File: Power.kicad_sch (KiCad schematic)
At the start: 12 parts

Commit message: finished power schematic
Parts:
- added C10, C11, C12, C9: 220pF, Capacitor_SMD:C_1210_3225Metric, symbol Device:C
- added Q1, Q2: IMZA65R050M2H, mosfets:TO247-4-Horizontal, symbol Library-N2-MOSFETs:IMZA65R050M2H
- added R1, R2: 50, Resistor_SMD:R_0805_2012Metric, symbol Device:R
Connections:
- net +15V_Top: no longer C8.1, PS2.6 (+Vo)
- net SW: now also Q1.2 (SOURCE1), Q2.1 (DRAIN); no longer C7.2, C8.2, PS2.4 (0V)
- new net: Q2.4 (GATE), R2.2
- new net: Q1.4 (GATE), R1.2
- new net +15V_Bot: C8.1, PS2.6 (+Vo)
- new net Bot_MOS_G: Q2.3 (SOURCE2), R2.1
- new net GNDPWR: C10.1, C11.1, C12.1, C7.2, C8.2, C9.1, PS2.4 (0V), Q2.2 (SOURCE1)
- new net HVBUS: C10.2, C11.2, C12.2, C9.2, Q1.1 (DRAIN)
- new net Top_MOS_G: Q1.3 (SOURCE2), R1.1
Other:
- moved on the sheet: C1, C2, C3, C4, C5, C6, C7, C8, L1, L2, PS1, PS2

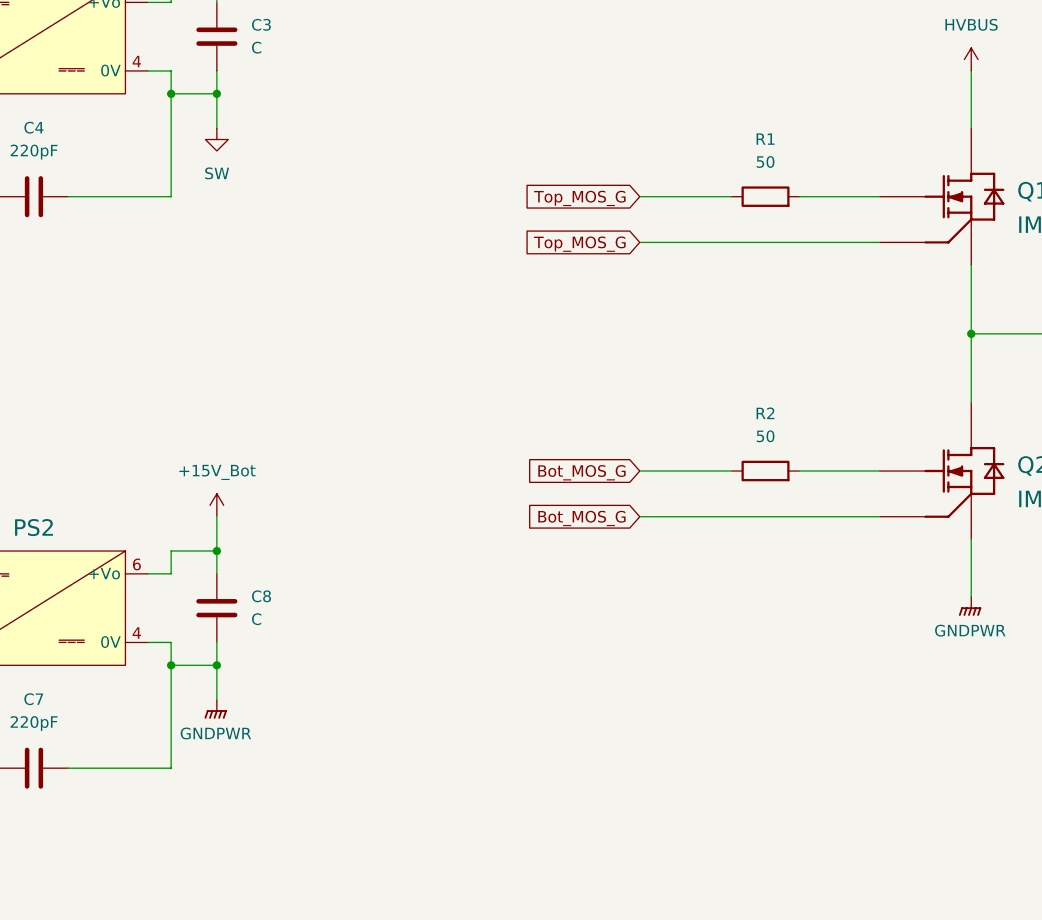
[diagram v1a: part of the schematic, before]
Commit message: gate driver added
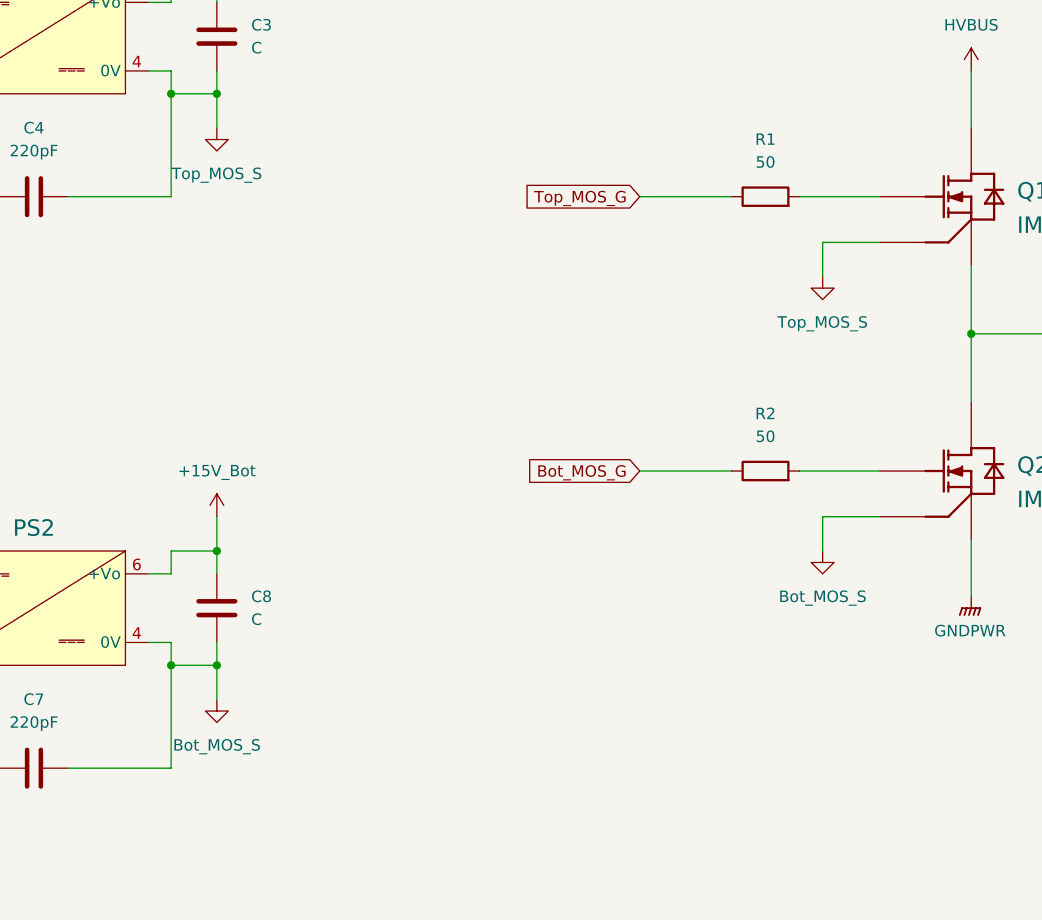
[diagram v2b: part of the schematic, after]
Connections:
- net Bot_MOS_G: no longer Q2.3 (SOURCE2)
- net GNDPWR: no longer C7.2, C8.2, PS2.4 (0V)
- net SW: no longer C3.2, C4.2, PS1.4 (0V)
- net Top_MOS_G: no longer Q1.3 (SOURCE2)
- new net Bot_MOS_S: C7.2, C8.2, PS2.4 (0V), Q2.3 (SOURCE2)
- new net Top_MOS_S: C3.2, C4.2, PS1.4 (0V), Q1.3 (SOURCE2)
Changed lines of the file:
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@@
+	(wire
+		(pts
+			(xy 198.12 107.95) (xy 204.47 107.95)
+		)
+		(stroke
+			(width 0)
+			(type default)
+		)
+	)
 	(wire
 		(pts
@@
 	(wire
 		(pts
+			(xy 198.12 77.47) (xy 204.47 77.47)
+		)
+		(stroke
+			(width 0)
+			(type default)
+		)
+	)
+	(wire
+		(pts
 			(xy 95.25 50.8) (xy 95.25 48.26)
 		)
@@
 	(wire
 		(pts
+			(xy 198.12 111.76) (xy 198.12 107.95)
+		)
+		(stroke
+			(width 0)
+			(type default)
+		)
+	)
+	(wire
+		(pts
 			(xy 123.19 114.3) (xy 125.73 114.3)
 		)
@@
 	(wire
 		(pts
+			(xy 198.12 81.28) (xy 198.12 77.47)
+		)
+		(stroke
+			(width 0)
+			(type default)
+		)
+	)
+	(wire
+		(pts
 			(xy 101.6 165.1) (xy 114.3 165.1)
 		)
@@
 	(wire
 		(pts
-			(xy 177.8 77.47) (xy 204.47 77.47)
-		)
-		(stroke
-			(width 0)
-			(type default)
-		)
-	)
-	(wire
-		(pts
 			(xy 130.81 111.76) (xy 130.81 107.95)
 		)
@@
 		(pts
 			(xy 101.6 175.26) (xy 101.6 177.8)
-		)
-		(stroke
-			(width 0)
-			(type default)
-		)
-	)
-	(wire
-		(pts
-			(xy 177.8 107.95) (xy 204.47 107.95)
 		)
 		(stroke
@@
 	(global_label "Bot_MOS_G"
 		(shape input)
-		(at 177.8 107.95 180)
+		(at 177.8 102.87 180)
 		(fields_autoplaced yes)
 		(effects
@@
 		)
 		(property "Intersheetrefs" "${INTERSHEET_REFS}"
-			(at 164.4735 107.95 0)
+			(at 164.4735 102.87 0)
 			(effects
 				(font
@@
 		)
 	)
-	(global_label "Bot_MOS_G"
+	(global_label "Top_MOS_G"
 		(shape input)
-		(at 177.8 102.87 180)
+		(at 177.8 72.39 180)
 		(fields_autoplaced yes)
 		(effects
@@
 		)
 		(property "Intersheetrefs" "${INTERSHEET_REFS}"
-			(at 164.4735 102.87 0)
+			(at 164.3526 72.39 0)
 			(effects
 				(font
@@
 		)
 	)
-	(global_label "Top_MOS_G"
+	(global_label "SW"
 		(shape input)
-		(at 177.8 72.39 180)
+		(at 229.87 87.63 0)
 		(fields_autoplaced yes)
 		(effects
@@
 				(size 1.27 1.27)
 			)
-			(justify right)
-		)
-		(property "Intersheetrefs" "${INTERSHEET_REFS}"
-			(at 164.3526 72.39 0)
-			(effects
-				(font
-					(size 1.27 1.27)
-				)
-				(justify right)
-				(hide yes)
-			)
-		)
-	)
-	(global_label "SW"
-		(shape input)
-		(at 229.87 87.63 0)
-		(fields_autoplaced yes)
-		(effects
-			(font
-				(size 1.27 1.27)
-			)
 			(justify left)
 		)
@@
 				)
 				(justify left)
-				(hide yes)
-			)
-		)
-	)
-	(global_label "Top_MOS_G"
-		(shape input)
-		(at 177.8 77.47 180)
-		(fields_autoplaced yes)
-		(effects
-			(font
-				(size 1.27 1.27)
-			)
-			(justify right)
-		)
-		(property "Intersheetrefs" "${INTERSHEET_REFS}"
-			(at 164.3526 77.47 0)
-			(effects
-				(font
-					(size 1.27 1.27)
-				)
-				(justify right)
 				(hide yes)
 			)
@@
 	)
 	(symbol
+		(lib_id "power:GND")
+		(at 198.12 81.28 0)
+		(unit 1)
+		(exclude_from_sim no)
+		(in_bom yes)
+		(on_board yes)
+		(dnp no)
+		(fields_autoplaced yes)
+		(property "Reference" "#PWR013"
+			(at 198.12 87.63 0)
+			(effects
+				(font
+					(size 1.27 1.27)
+				)
+				(hide yes)
+			)
+		)
+		(property "Value" "Top_MOS_S"
+			(at 198.12 86.36 0)
+			(effects
+				(font
+					(size 1.27 1.27)
+				)
+			)
+		)
+		(property "Footprint" ""
+			(at 198.12 81.28 0)
+			(effects
+				(font
+					(size 1.27 1.27)
+				)
+				(hide yes)
+			)
+		)
+		(property "Datasheet" ""
+			(at 198.12 81.28 0)
+			(effects
+				(font
+					(size 1.27 1.27)
+				)
+				(hide yes)
+			)
+		)
+		(property "Description" "Power symbol creates a global label with name \"GND\" , ground"
+			(at 198.12 81.28 0)
+			(effects
+				(font
+					(size 1.27 1.27)
+				)
+				(hide yes)
+			)
+		)
+		(pin "1"
+		)
+		(instances
+			(project "to247-4_card"
+				(path "/b6582af5-6107-4ea5-94ab-56651da9db37/c6f9b239-fb2c-4550-a056-6f105d804563"
+					(reference "#PWR013")
+					(unit 1)
+				)
+			)
+		)
+	)
+	(symbol
 		(lib_id "power:GNDPWR")
 		(at 214.63 116.84 0)
@@
 			)
 		)
-		(property "Value" "SW"
+		(property "Value" "Top_MOS_S"
 			(at 130.81 69.85 0)
 			(effects
@@
 				(path "/b6582af5-6107-4ea5-94ab-56651da9db37/c6f9b239-fb2c-4550-a056-6f105d804563"
 					(reference "#PWR04")
-					(unit 1)
-				)
-			)
-		)
-	)
-	(symbol
-		(lib_id "power:GNDPWR")
-		(at 130.81 128.27 0)
-		(unit 1)
-		(exclude_from_sim no)
-		(in_bom yes)
-		(on_board yes)
-		(dnp no)
-		(fields_autoplaced yes)
-		(property "Reference" "#PWR08"
-			(at 130.81 133.35 0)
-			(effects
-				(font
-					(size 1.27 1.27)
-				)
-				(hide yes)
-			)
-		)
-		(property "Value" "GNDPWR"
-			(at 130.683 132.08 0)
-			(effects
-				(font
-					(size 1.27 1.27)
-				)
-			)
-		)
-		(property "Footprint" ""
-			(at 130.81 129.54 0)
-			(effects
-				(font
-					(size 1.27 1.27)
-				)
-				(hide yes)
-			)
-		)
-		(property "Datasheet" ""
-			(at 130.81 129.54 0)
-			(effects
-				(font
-					(size 1.27 1.27)
-				)
-				(hide yes)
-			)
-		)
-		(property "Description" "Power symbol creates a global label with name \"GNDPWR\" , global ground"
-			(at 130.81 128.27 0)
-			(effects
-				(font
-					(size 1.27 1.27)
-				)
-				(hide yes)
-			)
-		)
-		(pin "1"
-		)
-		(instances
-			(project ""
-				(path "/b6582af5-6107-4ea5-94ab-56651da9db37/c6f9b239-fb2c-4550-a056-6f105d804563"
-					(reference "#PWR08")
 					(unit 1)
 				)
@@
 	)
 	(symbol
+		(lib_id "power:GND")
+		(at 130.81 128.27 0)
+		(unit 1)
+		(exclude_from_sim no)
+		(in_bom yes)
+		(on_board yes)
+		(dnp no)
+		(fields_autoplaced yes)
+		(property "Reference" "#PWR08"
+			(at 130.81 134.62 0)
+			(effects
+				(font
+					(size 1.27 1.27)
+				)
+				(hide yes)
+			)
+		)
+		(property "Value" "Bot_MOS_S"
+			(at 130.81 133.35 0)
+			(effects
+				(font
+					(size 1.27 1.27)
+				)
+			)
+		)
+		(property "Footprint" ""
+			(at 130.81 128.27 0)
+			(effects
+				(font
+					(size 1.27 1.27)
+				)
+				(hide yes)
+			)
+		)
+		(property "Datasheet" ""
+			(at 130.81 128.27 0)
+			(effects
+				(font
+					(size 1.27 1.27)
+				)
+				(hide yes)
+			)
+		)
+		(property "Description" "Power symbol creates a global label with name \"GND\" , ground"
+			(at 130.81 128.27 0)
+			(effects
+				(font
+					(size 1.27 1.27)
+				)
+				(hide yes)
+			)
+		)
+		(pin "1"
+		)
+		(instances
+			(project "to247-4_card"
+				(path "/b6582af5-6107-4ea5-94ab-56651da9db37/c6f9b239-fb2c-4550-a056-6f105d804563"
+					(reference "#PWR08")
+					(unit 1)
+				)
+			)
+		)
+	)
+	(symbol
 		(lib_id "power:VBUS")
 		(at 214.63 58.42 0)
@@
 					(unit 1)
 				)
+			)
+		)
+	)
+	(symbol
+		(lib_id "power:GND")
+		(at 198.12 111.76 0)
+		(unit 1)
+		(exclude_from_sim no)
+		(in_bom yes)
+		(on_board yes)
+		(dnp no)
+		(fields_autoplaced yes)
+		(property "Reference" "#PWR014"
+			(at 198.12 118.11 0)
+			(effects
+				(font
+					(size 1.27 1.27)
+				)
+				(hide yes)
+			)
+		)
+		(property "Value" "Bot_MOS_S"
+			(at 198.12 116.84 0)
+			(effects
+				(font
+					(size 1.27 1.27)
+				)
+			)
+		)
+		(property "Footprint" ""
+			(at 198.12 111.76 0)
+			(effects
+				(font
+					(size 1.27 1.27)
+				)
+				(hide yes)
+			)
+		)
+		(property "Datasheet" ""
+			(at 198.12 111.76 0)
+			(effects
+				(font
+					(size 1.27 1.27)
+				)
+				(hide yes)
+			)
+		)
+		(property "Description" "Power symbol creates a global label with name \"GND\" , ground"
+			(at 198.12 111.76 0)
+			(effects
+				(font
+					(size 1.27 1.27)
+				)
+				(hide yes)
+			)
+		)
+		(pin "1"
+		)
+		(instances
+			(project "to247-4_card"
+				(path "/b6582af5-6107-4ea5-94ab-56651da9db37/c6f9b239-fb2c-4550-a056-6f105d804563"
+					(reference "#PWR014")
+					(unit 1)
+				)

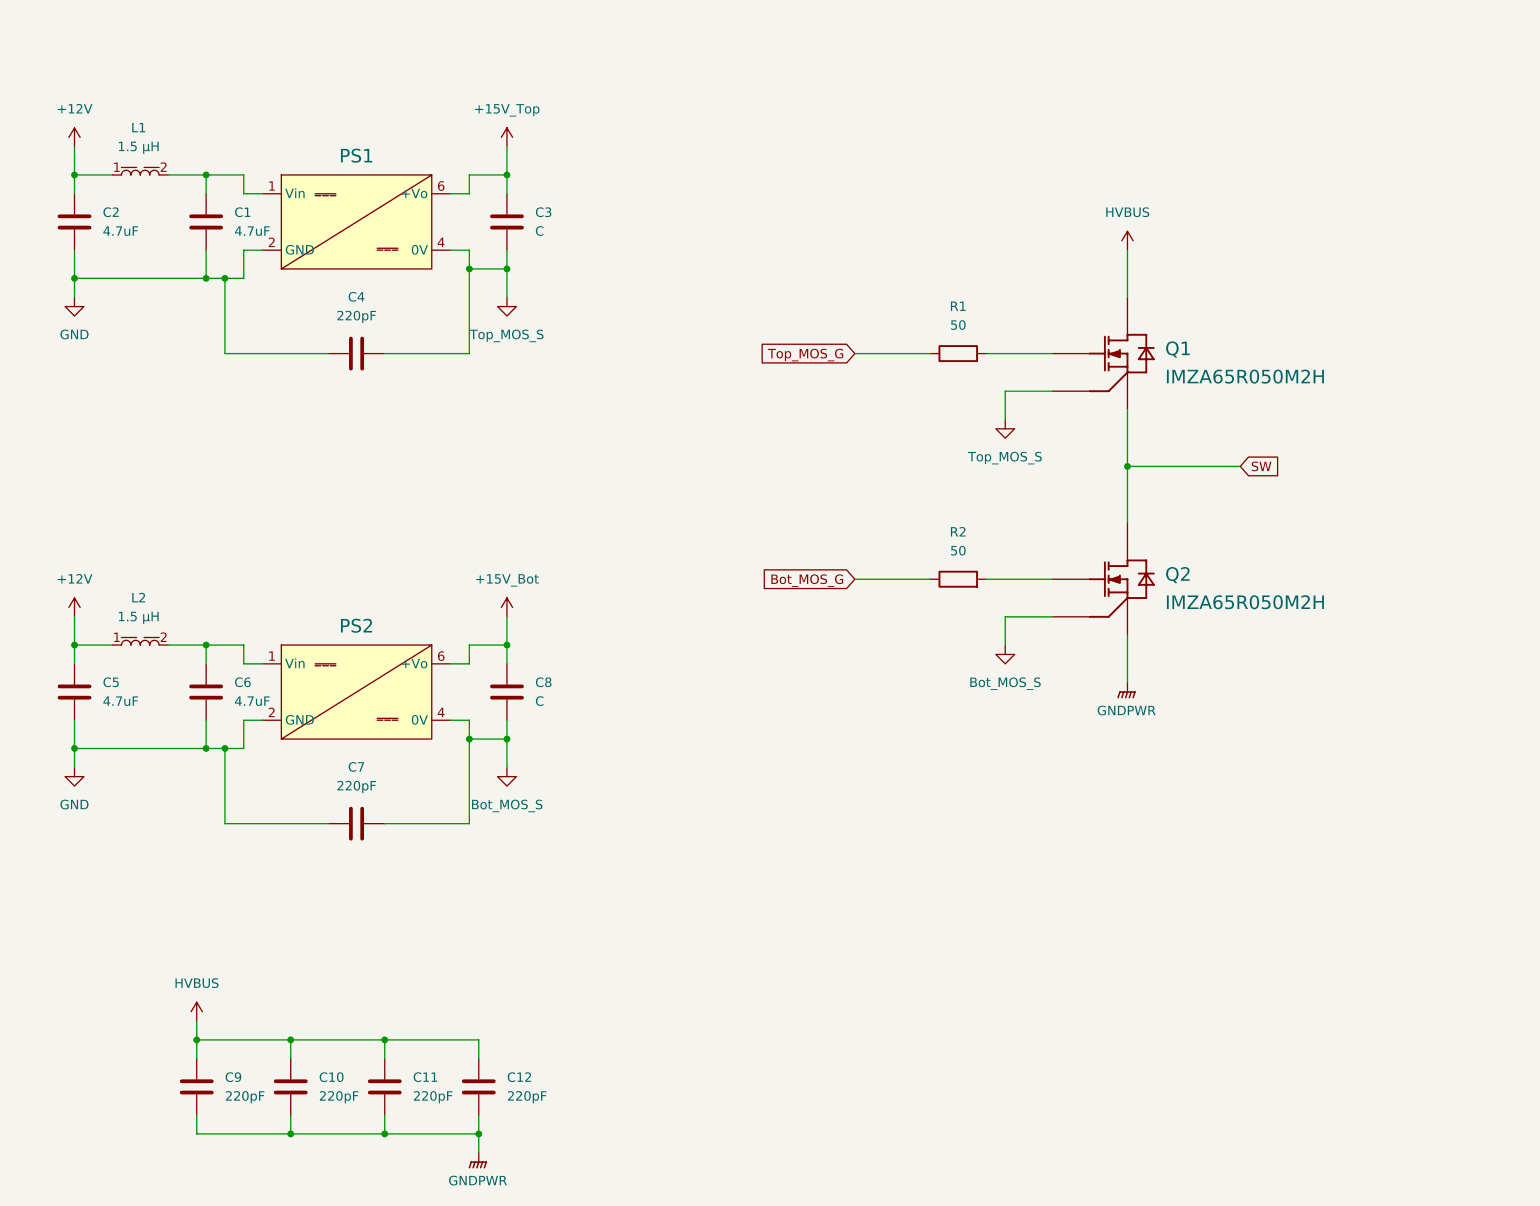
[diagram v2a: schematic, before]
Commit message: added LM1117-5.0
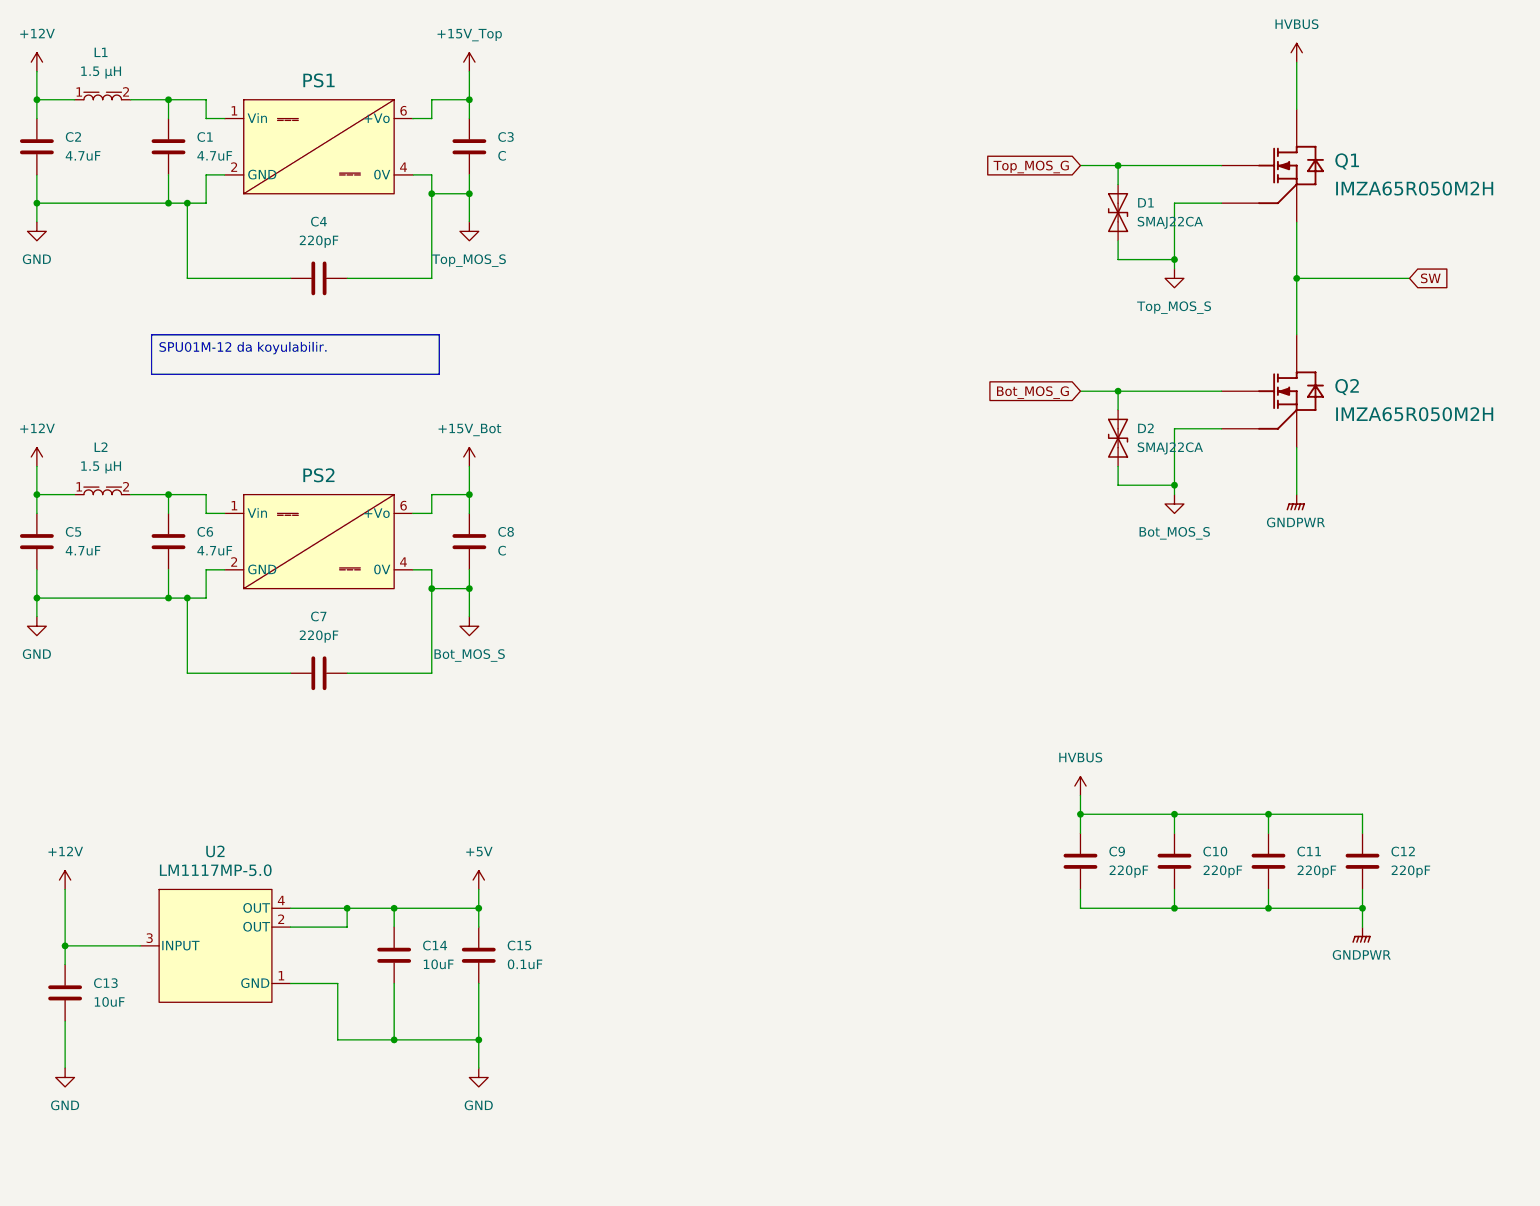
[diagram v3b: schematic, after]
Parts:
- removed R1, R2: 50, Resistor_SMD:R_0805_2012Metric, symbol Device:R
- added C13, C14: 10uF, Capacitor_SMD:C_0805_2012Metric, symbol Device:C
- added C15: 0.1uF, Capacitor_SMD:C_0805_2012Metric, symbol Device:C
- added D1, D2: SMAJ22CA, Diode_SMD:D_SMA, symbol Diode:SMAJ22CA
- added U2: LM1117MP-5.0, DCDC-converters:DCY0004A_M, symbol Library-N3-DCDC-Converters:LM1117MP-5.0
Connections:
- net +12V: now also C13.1, U2.3 (INPUT)
- net Bot_MOS_G: now also Q2.4 (GATE), D2.2 (A2)
- net Bot_MOS_S: now also D2.1 (A1)
- net GND: now also C13.2, C14.2, C15.2, U2.1 (GND)
- net Top_MOS_G: now also Q1.4 (GATE), D1.2 (A2)
- net Top_MOS_S: now also D1.1 (A1)
- new net +5V: C14.1, C15.1, U2.2 (OUT), U2.4 (OUT)
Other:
- moved on the sheet: C1, C10, C11, C12, C2, C3, C4, C5, C6, C7, C8, C9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
